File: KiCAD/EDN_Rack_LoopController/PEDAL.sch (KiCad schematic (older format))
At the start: 127 parts, among them J1 XLR3, SW1 SW_Push_DPDT, SW2 SW_Push_DPDT, SW3 SW_Push_DPDT, SW4 SW_Push_DPDT, SW5 SW_Push_DPDT, SW6 SW_Push_DPDT, SW7 SW_Push_DPDT, SW8 SW_Push_DPDT, U1 L7805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

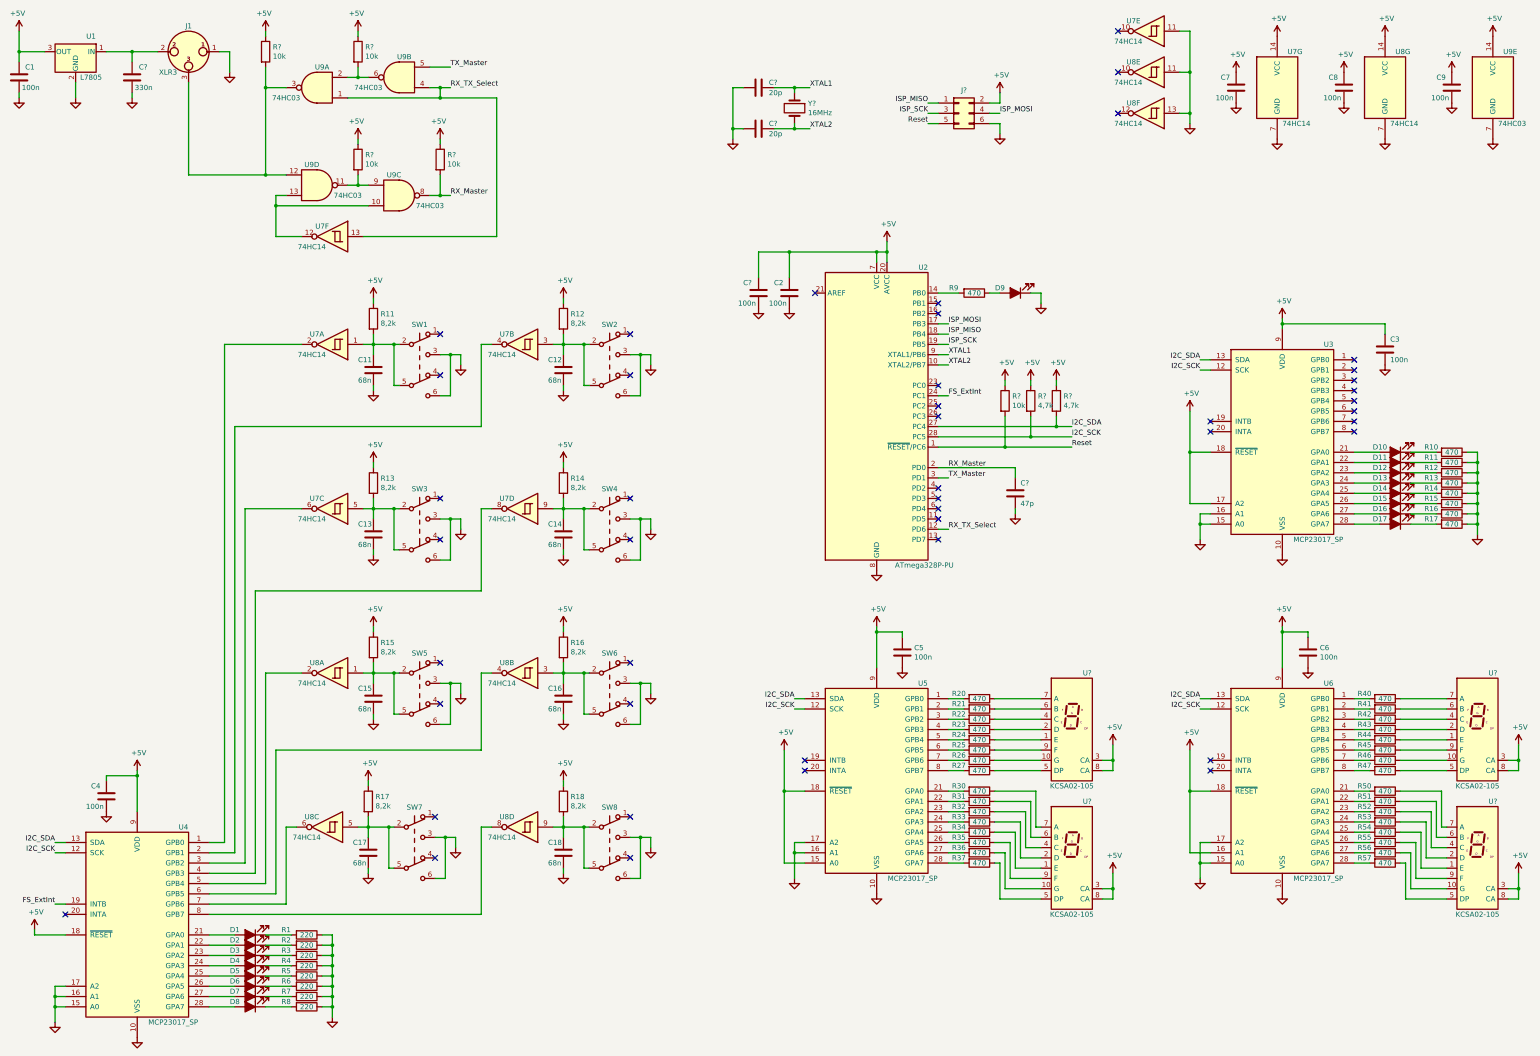
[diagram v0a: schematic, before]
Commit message: Schematic polish, added complete schematic pdf.
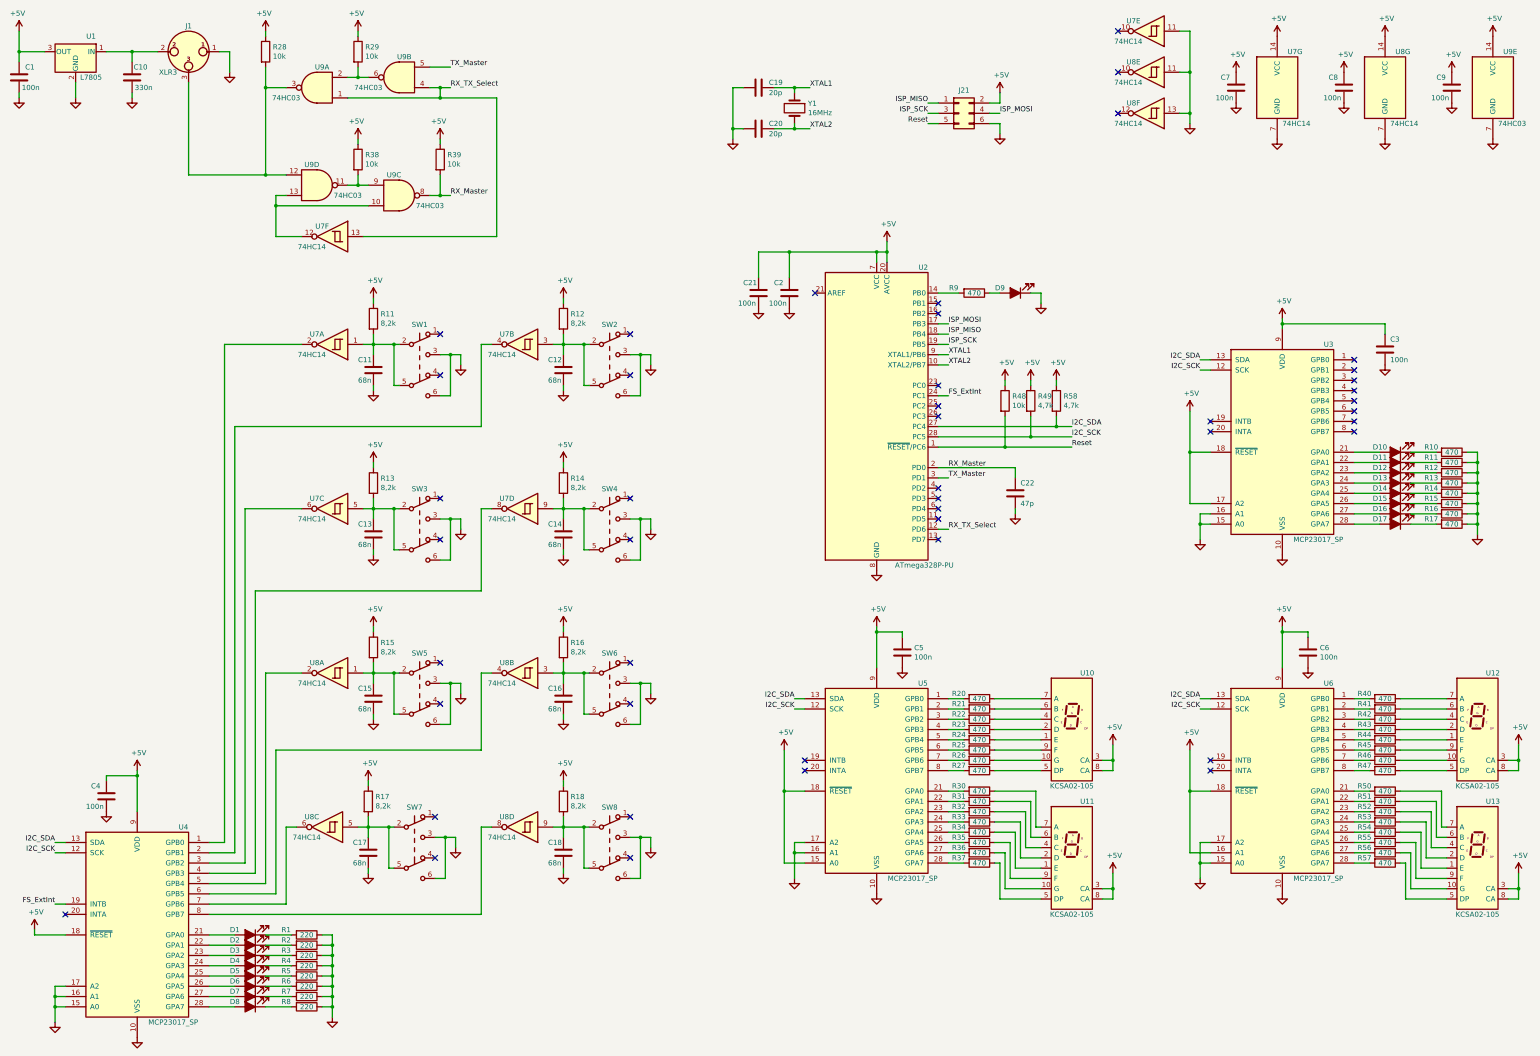
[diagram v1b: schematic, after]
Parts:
- gave numbers to parts that had none: 18
